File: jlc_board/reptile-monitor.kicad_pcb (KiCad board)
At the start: 4 copper layers, 38.1 x 76.2 mm, 49 parts, among them J1 USB_C_Receptacle_USB2.0, J2 AC_IN, J3 Conn_01x08, J7 LOAD0, J8 LOAD1, K1 1462041-7, K2 1462041-7, SW1 RESET, SW2 BOOT, U1 ESP32-S2-WROVER, U2 TPS2112PW, U3 AP2112K-3.3, U4 MDC3105LT1G, U5 MDC3105LT1G, Y1 32.768KHz 12.5p

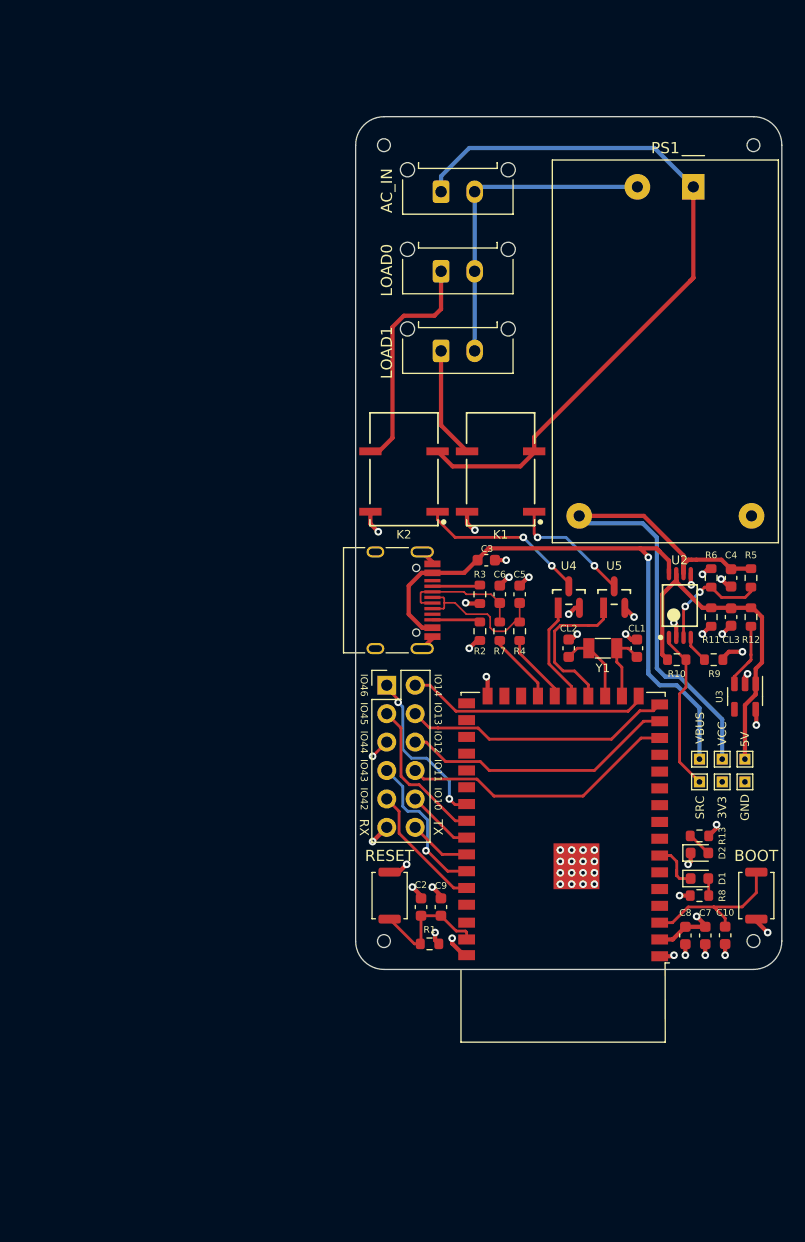
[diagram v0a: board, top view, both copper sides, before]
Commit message: Rev2 - Change to Panasonic relays as they're actually attainable and cheaper.
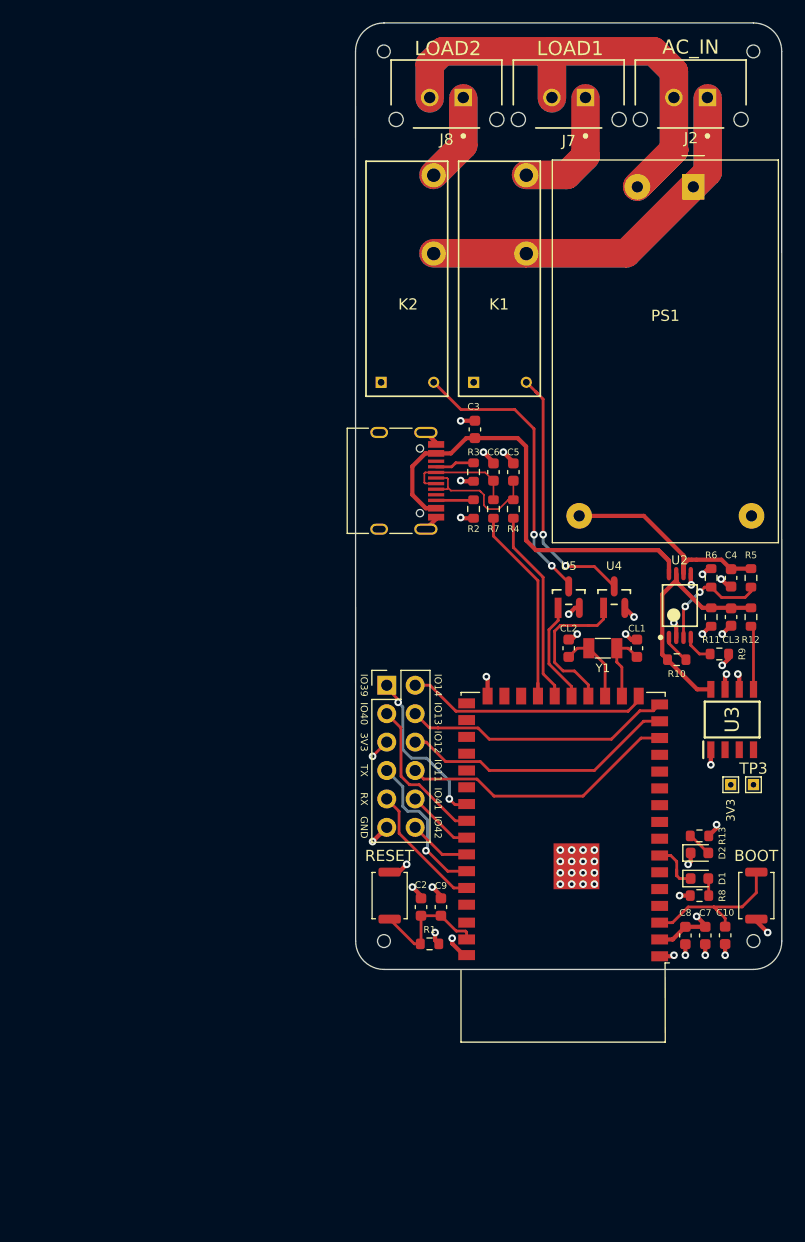
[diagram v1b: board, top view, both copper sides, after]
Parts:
- removed TP2: SRC, TestPoint:TestPoint_THTPad_1.0x1.0mm_Drill0.5mm
- removed TP4: 5V, TestPoint:TestPoint_THTPad_1.0x1.0mm_Drill0.5mm
- removed TP5: VCC, TestPoint:TestPoint_THTPad_1.0x1.0mm_Drill0.5mm
- removed TP6: VBUS, TestPoint:TestPoint_THTPad_1.0x1.0mm_Drill0.5mm
- J2: footprint Connector_Molex:Molex_Micro-Fit_3.0_43650-0215_1x02_P3.00mm_Vertical -> reptile-monitor:Molex-43650-0215-0-0-MFG
- J7: value LOAD0 -> LOAD1; footprint Connector_Molex:Molex_Micro-Fit_3.0_43650-0215_1x02_P3.00mm_Vertical -> reptile-monitor:Molex-43650-0215-0-0-MFG
- J8: value LOAD1 -> LOAD2; footprint Connector_Molex:Molex_Micro-Fit_3.0_43650-0215_1x02_P3.00mm_Vertical -> reptile-monitor:Molex-43650-0215-0-0-MFG
- K1, K2: value 1462041-7 -> ALDP105W; footprint Reptile_Monitor:TE_Connectivity-1462041-7-0-0 -> reptile-monitor:Panasonic-ALDP105W-Manufacturer_Recommended
- R10: value 10K -> 10k
- R9: value 500R -> 500r
- U3: footprint Package_TO_SOT_SMD:SOT-23-5 -> SamacSys_Parts:SOIC127P600X170-8N
- moved J2 24.0 mm to (161.3, 41.1)
- moved J8 23.0 mm to (139.4, 41.1)
- moved J7 19.5 mm to (150.4, 41.1)
- moved C3 11.7 mm to (142.0, 71.1), turned to 90 degrees
- moved C5 10.9 mm to (145.4, 74.9)
- moved C6 10.9 mm to (143.6, 74.9)
- moved R2 10.9 mm to (141.9, 78.2)
- moved R3 10.9 mm to (141.9, 74.9)
- moved R4 10.9 mm to (145.4, 78.2)
- moved R7 10.9 mm to (143.6, 78.2)
- moved J1 10.7 mm to (134.5, 75.7)
- moved K1 8.13 mm to (141.9, 66.9)
- moved K2 8.03 mm to (133.6, 66.9)
- moved U5 4.06 mm to (150.4, 86.1)
- moved U4 4.05 mm to (154.4, 86.1)
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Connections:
- J7 pad 1: /LOAD_0 -> /LOAD1
- J8 pad 1: /LOAD_1 -> /LOAD2
- K1 pad 1: Net-(K1-Pad1) -> GND
- K2 pad 1: Net-(K2-Pad1) -> GND
- R12 pad 1: +5V -> Net-(R12-Pad1)
- R12 pad 2: Net-(R12-Pad2) -> +5V
- U3 pad 1: +5V -> +3V3
- U3 pad 2: GND -> (no net)
- U3 pad 3: Net-(R12-Pad2) -> (no net)
- U3 pad 5: +3V3 -> Net-(R12-Pad1)
- U4 pad 1: /IO18 -> /IO17
- U4 pad 3: Net-(K2-Pad1) -> Net-(K1-Pad4)
- U5 pad 1: /IO17 -> /IO18
- U5 pad 3: Net-(K1-Pad1) -> Net-(K2-Pad4)
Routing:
- net /AC_N: track 29.6 -> 280.0 mm
- net /AC_L: track 66.1 -> 204.7 mm
- net /LOAD1: track 0.00 -> 67.1 mm
- net /LOAD2: track 0.00 -> 47.7 mm
- net VCC: track 50.5 -> 19.8 mm
- net Net-(K2-Pad4): track 0.00 -> 26.1 mm, vias 0 -> 2
- net Net-(K1-Pad4): track 0.00 -> 23.2 mm, vias 0 -> 2
- net /LOAD_0: track 20.8 -> 0.00 mm
- net Net-(K2-Pad1): track 15.1 -> 0.00 mm, vias 2 -> 0
- net VBUS: track 53.7 -> 40.9 mm, vias 1 -> 0
- net Net-(R7-Pad2): track 6.38 -> 18.7 mm
- net /PWR_SRC: track 14.5 -> 2.65 mm
- net Net-(R4-Pad2): track 6.27 -> 18.1 mm
- net Net-(K1-Pad1): track 11.1 -> 0.00 mm, vias 2 -> 0
- net /LOAD_1: track 9.94 -> 0.00 mm
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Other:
- board size 38.1 x 76.2 mm -> 38.1 x 84.6 mm
- board text added: "3V3"
- board text added: "ESP32-S2 Reptile Monitor Mike Pleimann Rev 2 April 2021"
- board text added: "GND"
- board text added: "IO39"
- board text added: "IO40"
- board text added: "IO41"
- board text removed: "ESP32-S2 Reptile Monitor Mike Pleimann v1.0 April 2021"
- board text removed: "IO10"
- board text removed: "IO43"
- board text removed: "IO44"
- board text removed: "IO45"
- board text removed: "IO46"

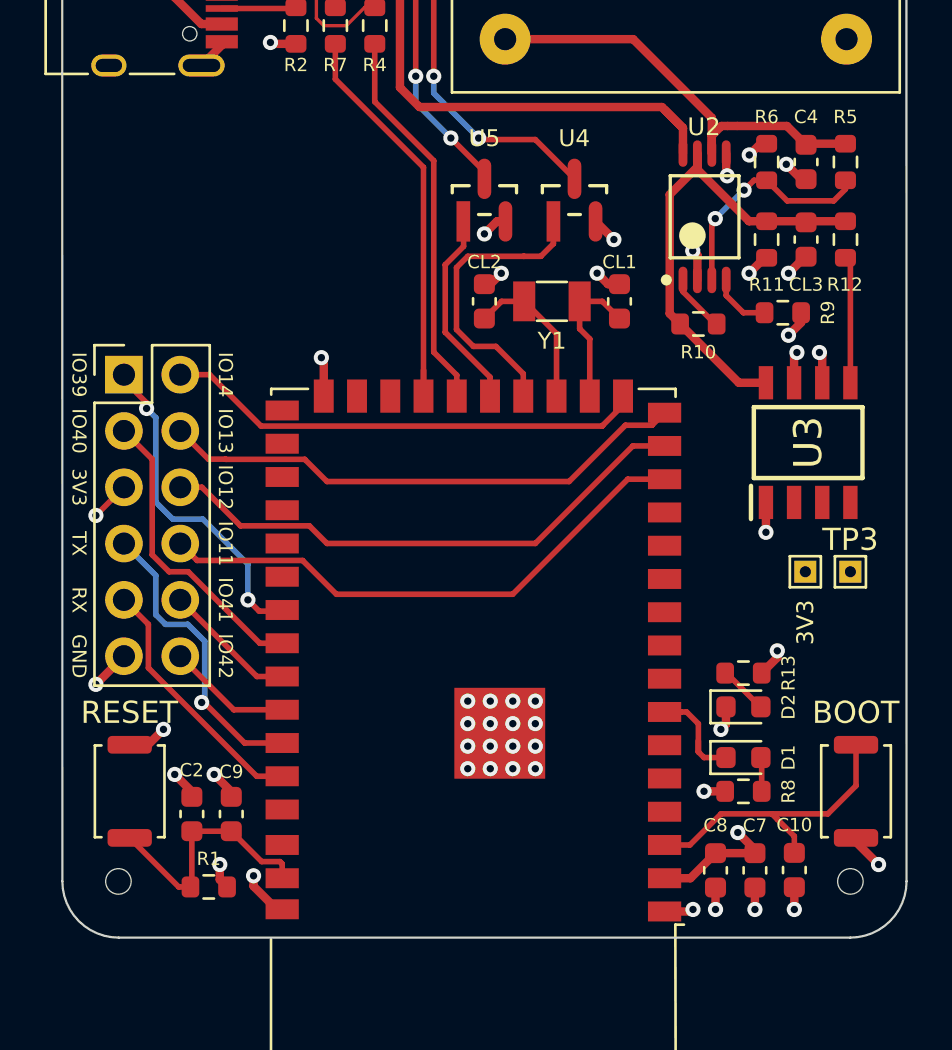
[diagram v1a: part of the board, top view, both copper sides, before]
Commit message: Change ALPS to Omron boot and reset buttons cause they're available from Digi-Key
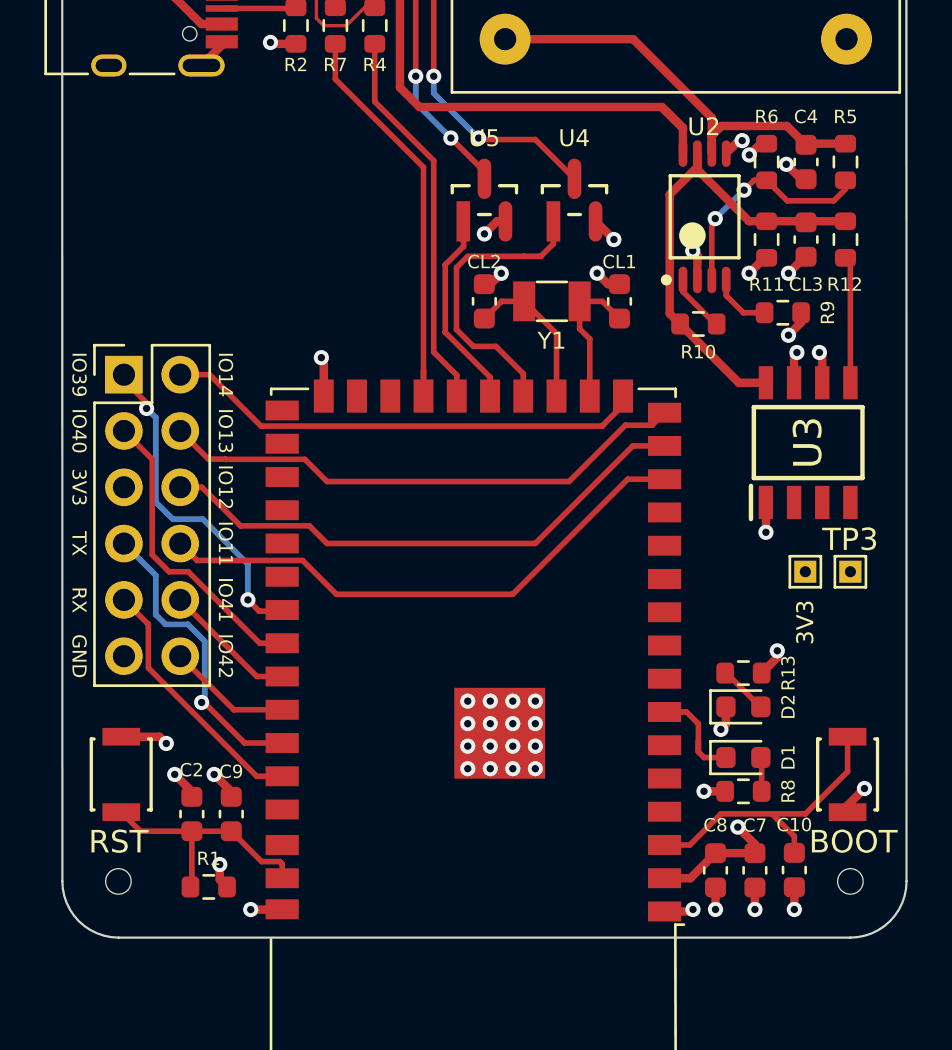
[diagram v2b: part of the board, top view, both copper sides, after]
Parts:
- SW1: value RESET -> RST; footprint Reptile_Monitor:Alps_SKRK -> reptile-monitor:Omron-B3U-1000P-MFG
- SW2: footprint Reptile_Monitor:Alps_SKRK -> reptile-monitor:Omron-B3U-1000P-MFG
- moved SW1 0.85 mm to (134.0, 112.0), turned to 90 degrees
- moved SW2 0.85 mm to (166.8, 112.0), turned to -90 degrees
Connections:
- SW1 pad 1: GND -> /EN
- SW1 pad 2: /EN -> GND
- SW2 pad 1: GND -> /IO0
- SW2 pad 2: /IO0 -> GND
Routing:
- net GND: track 42.9 -> 40.4 mm, vias 47 -> 46
- net +3V3: track 11.3 -> 9.79 mm, vias 5 -> 4

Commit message: rev2
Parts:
- removed C3, C4: 0.1u, Capacitor_SMD:C_0603_1608Metric
- removed C5, C6: 20p, Capacitor_SMD:C_0603_1608Metric
- removed CL3: 10u, Capacitor_SMD:C_0603_1608Metric
- removed R10, R11: 10k, Resistor_SMD:R_0603_1608Metric
- removed R2, R3: 5.1k, Resistor_SMD:R_0603_1608Metric
- removed R4, R7: 22r, Resistor_SMD:R_0603_1608Metric
- removed R5: 2.2k, Resistor_SMD:R_0603_1608Metric
- removed R6: 1k, Resistor_SMD:R_0603_1608Metric
- removed R9: 500r, Resistor_SMD:R_0603_1608Metric
- removed TP1: 3V3, TestPoint:TestPoint_THTPad_1.0x1.0mm_Drill0.5mm
- removed TP3: GND, TestPoint:TestPoint_THTPad_1.0x1.0mm_Drill0.5mm
- removed U2: TPS2112PW, Reptile_Monitor:Texas_Instruments-TPS2112PW
- removed U4, U5: MDC3105LT1G, Reptile_Monitor:ON_Semiconductor-318-08-01_2018-AS
- added C1: 1u, Capacitor_SMD:C_0805_2012Metric, F.Cu at (161.2, 87.4)
- added F1: 39215000000, SamacSys_Parts:TO508P400X850X850-2P, F.Cu at (167.0, 45.8)
- added IC1: ESP32-WROVER-E_M213EH6464PH3Q0_, SamacSys_Parts:ESP32WROVEREM213EH6464PH3Q0, F.Cu at (149.9, 109.9)
- added REF1: MountingHole_2.2mm_M2, MountingHole:MountingHole_2.2mm_M2, F.Cu at (166.4, 55.1)
- added REF1: MountingHole_2.2mm_M2, MountingHole:MountingHole_2.2mm_M2, F.Cu at (133.9, 45.0)
- added REF2: MountingHole_2.2mm_M2, MountingHole:MountingHole_2.2mm_M2, F.Cu at (133.9, 116.8)
- added REF3: MountingHole_2.2mm_M2, MountingHole:MountingHole_2.2mm_M2, F.Cu at (166.9, 116.8)
- added RV1: Varistor, Varistor:RV_Disc_D7mm_W3.4mm_P5mm, F.Cu at (153.5, 45.5)
- added WAFFLE: LOGO, LOGO, B.Cu at (151.3, 105.7)
- added WESLEY: LOGO, LOGO, B.Cu at (142.0, 78.1)
- added svg2mod: G***, svg2mod, B.Cu at (159.8, 74.8)
- added svg2mod: G***, svg2mod, B.Cu at (154.8, 85.2)
- C2: value 0.1u -> 1u; footprint Capacitor_SMD:C_0603_1608Metric -> Capacitor_SMD:C_0805_2012Metric
- J1: value USB_C_Receptacle_USB2.0 -> UART; footprint Reptile_Monitor:USB_C_Receptacle_HRO_TYPE-C-31-M-12 -> Connector_PinHeader_2.54mm:PinHeader_1x04_P2.54mm_Vertical
- U1: value ESP32-S2-WROVER -> NUD3105DMT1G; footprint RF_Module:ESP32-S2-WROVER -> reptile-monitor:ON_Semi-318F-0-0-0
- Y1: footprint Reptile_Monitor:Crystal_SMD_3215-2Pin_3.2x1.5mm -> reptile-monitor:Crystal_SMD_3215-2Pin_3.2x1.5mm
- moved C2 33.1 mm to (161.2, 90.9), turned to -90 degrees
- moved SW1 33.0 mm to (167.0, 112.3), turned to -90 degrees
- moved SW2 32.9 mm to (133.9, 112.3)
- moved C10 27.9 mm to (136.7, 112.8)
- moved C9 24.8 mm to (163.7, 112.0), turned to -90 degrees
- moved R1 24.4 mm to (161.8, 112.0), turned to 90 degrees
- moved J1 24.1 mm to (135.4, 99.8), turned to 0 degrees
- moved CL2 21.5 mm to (165.1, 106.3), turned to 0 degrees
- moved CL1 19.7 mm to (165.1, 108.3), turned to 0 degrees
- moved U1 19.5 mm to (153.3, 87.2), turned to 0 degrees
- moved Y1 18.8 mm to (162.2, 107.3), turned to 90 degrees
- moved R8 12.3 mm to (163.7, 100.6), turned to -90 degrees
- moved D1 10.7 mm to (162.2, 100.6), turned to 90 degrees
- moved D2 9.21 mm to (165.9, 100.6), turned to 90 degrees
- moved R13 8.69 mm to (167.4, 100.6), turned to 90 degrees
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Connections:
- net Net-(R12-Pad1) renamed /PWR_EN
- C2 pad 1: /EN -> GND
- C2 pad 2: GND -> +3V3
- C9 pad 1: /EN -> Net-(C9-Pad1)
- CL1 pad 1: /IO15 -> Net-(CL1-Pad1)
- CL2 pad 1: /IO16 -> Net-(CL2-Pad1)
- D1 pad 1: Net-(D1-Pad1) -> /IO13
- J3 pad 1: /IO39 -> /IO18
- J3 pad 10: /IO41 -> /IO25
- J3 pad 11: GND -> /IO26
- J3 pad 12: /IO42 -> /IO27
- J3 pad 2: /IO14 -> /IO19
- J3 pad 3: /IO40 -> /IO15
- J3 pad 4: /IO13 -> /IO5
- J3 pad 5: +3V3 -> /IO21
- J3 pad 6: /IO12 -> /IO22
- J3 pad 7: /TXD0 -> /IO23
- J3 pad 8: /IO11 -> /IO36
- J3 pad 9: /RXD0 -> /IO39
- K1 pad 1: GND -> +5V
- K1 pad 3: /AC_L -> /FUSED_AC_L
- K1 pad 4: Net-(K1-Pad4) -> /RLY1
- K2 pad 1: GND -> +5V
- K2 pad 3: /AC_L -> /FUSED_AC_L
- K2 pad 4: Net-(K2-Pad4) -> /RLY2
- PS1 pad 1: /AC_L -> /FUSED_AC_L
- PS1 pad 4: VCC -> +5V
- R1 pad 1: +3V3 -> /EN
- R1 pad 2: /EN -> Net-(C9-Pad1)
- SW1 pad 1: /EN -> Net-(C9-Pad1)
- U1 pad 2: +3V3 -> /IO14
- U1 pad 3: /IO0 -> /RLY2
- U1 pad 4: (no net) -> GND
- U1 pad 5: (no net) -> /IO12
- U1 pad 6: (no net) -> /RLY1
- U3 pad 2: (no net) -> unconnected-(U3-Pad2)
- U3 pad 3: (no net) -> unconnected-(U3-Pad3)
- U3 pad 4: (no net) -> unconnected-(U3-Pad4)
- Y1 pad 1: /IO16 -> Net-(CL2-Pad1)
- Y1 pad 2: /IO15 -> Net-(CL1-Pad1)
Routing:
- net /AC_N: track 280.0 -> 0.00 mm, vias 0 -> 27
- net /AC_L: track 204.7 -> 0.00 mm, vias 0 -> 7
- net /LOAD1: track 67.1 -> 0.00 mm, vias 0 -> 11
- net /LOAD2: track 47.7 -> 0.00 mm, vias 0 -> 10
- net VBUS: track 40.9 -> 0.00 mm
- net /IO36: track 0.00 -> 34.7 mm
- net /IO22: track 0.00 -> 31.8 mm
- net /IO23: track 0.00 -> 29.9 mm
- net /RLY2: track 0.00 -> 28.3 mm
- net /IO19: track 0.00 -> 26.6 mm
- net +5V: track 22.0 -> 48.1 mm
- net Net-(K2-Pad4): track 26.1 -> 0.00 mm, vias 2 -> 0
- net /IO25: track 0.00 -> 25.4 mm
- net /IO21: track 0.00 -> 25.2 mm
- net /RLY1: track 0.00 -> 25.1 mm
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- added copper zone on B.Cu, net /AC_L
- added copper zone on F.Cu, net /AC_L
- added copper zone on In1.Cu, net /AC_L
- added copper zone on In2.Cu, net /AC_L
- added copper zone on B.Cu, net /AC_N
- added copper zone on F.Cu, net /AC_N
- added copper zone on In1.Cu, net /AC_N
- added copper zone on In2.Cu, net /AC_N
- added copper zone on B.Cu, net /FUSED_AC_L
- added copper zone on F.Cu, net /FUSED_AC_L
- added copper zone on In1.Cu, net /FUSED_AC_L
- added copper zone on In2.Cu, net /FUSED_AC_L
- added copper zone on B.Cu, net /LOAD1
- added copper zone on F.Cu, net /LOAD1
- added copper zone on In1.Cu, net /LOAD1
- added copper zone on In2.Cu, net /LOAD1
- added copper zone on B.Cu, net /LOAD2
- added copper zone on F.Cu, net /LOAD2
- added copper zone on In1.Cu, net /LOAD2
- added copper zone on In2.Cu, net /LOAD2
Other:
- outline, holes or cut-outs redrawn
- board text added: "15"
- board text added: "18"
- board text added: "19"
- board text added: "21"
- board text added: "22"
- board text added: "23"
- board text added: "25"
- board text added: "26"
- board text added: "27"
- board text added: "36"
- board text added: "39"
- board text added: "5"
- board text added: "Rev 2 April 2021"
- board text removed: "ESP32-S2 Reptile Monitor Mike Pleimann Rev 2 April 2021"
- board text removed: "IO11"
- board text removed: "IO12"
- board text removed: "IO13"
- board text removed: "IO14"
- board text removed: "IO39"
- board text removed: "IO40"
- board text removed: "IO41"
- board text removed: "IO42"
